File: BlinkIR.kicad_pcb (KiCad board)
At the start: 2 copper layers, 12 parts, among them U1 ATtiny10-TS

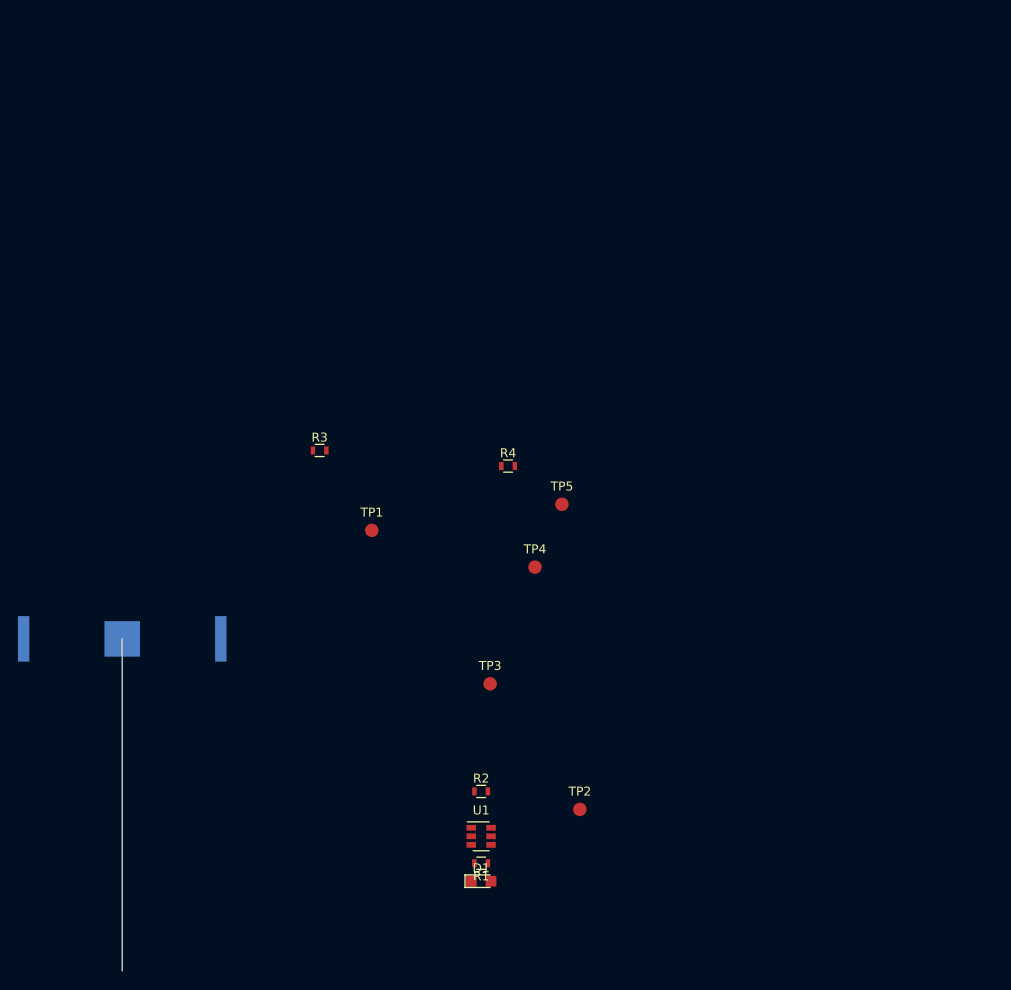
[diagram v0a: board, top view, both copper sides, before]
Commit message: software retargeted to ATTiny10 and dropped uart Schmatic work finished rev1
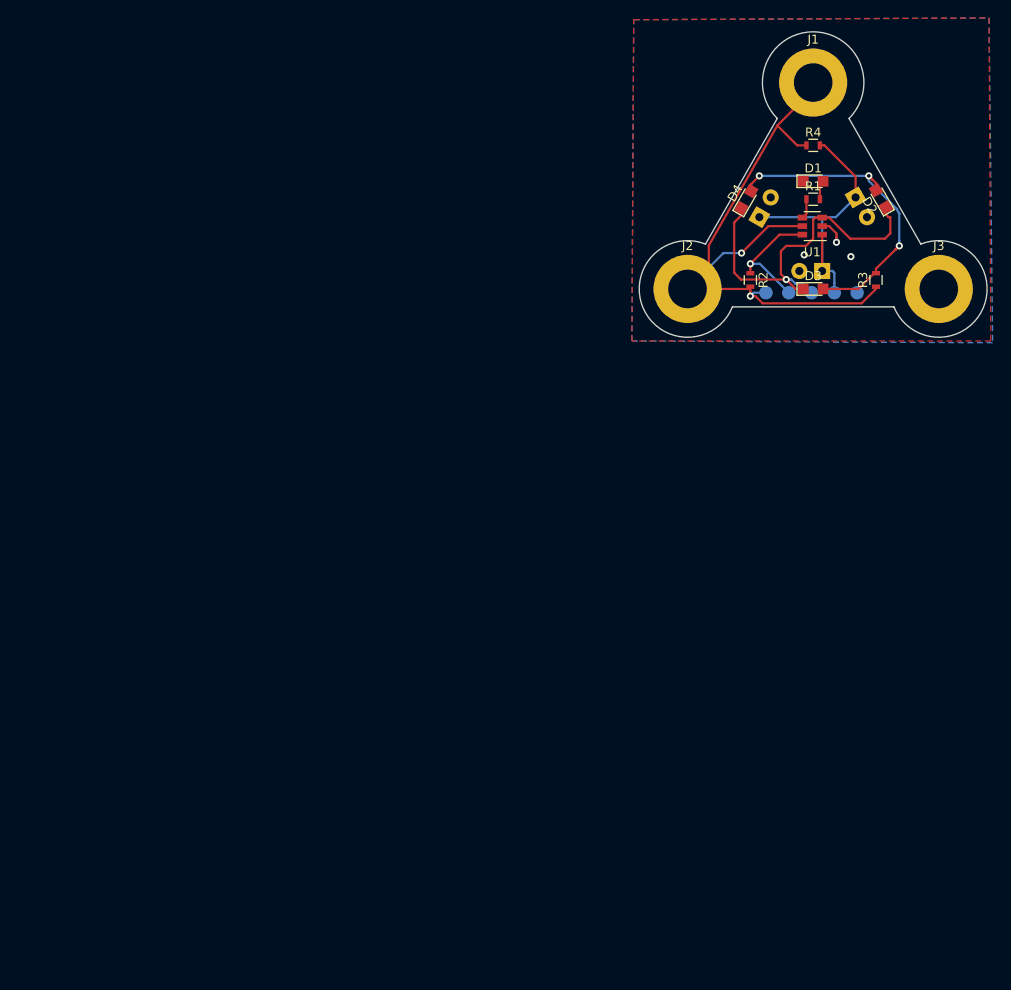
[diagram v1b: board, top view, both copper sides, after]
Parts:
- removed BT1: Battery_Cell, Battery_Holders:Keystone_3034_1x20mm-CoinCell
- added D2: LED, LEDs:LED_0805, F.Cu at (191.6, 64.0)
- added D3: LED, LEDs:LED_0805, F.Cu at (184.0, 74.0)
- added D4: LED, LEDs:LED_0805, F.Cu at (176.6, 64.0)
- added J1: Conn_01x01, Mounting_Holes:MountingHole_4.3mm_M4_ISO7380_Pad, F.Cu at (184.0, 51.0)
- added J2: Conn_01x01, Mounting_Holes:MountingHole_4.3mm_M4_ISO7380_Pad, F.Cu at (170.0, 74.0)
- added J3: Conn_01x01, Mounting_Holes:MountingHole_4.3mm_M4_ISO7380_Pad, F.Cu at (198.0, 74.0)
- added Q1: Q_Photo_NPN, LEDs:LED_D3.0mm_Horizontal_O1.27mm_Z2.0mm, B.Cu at (185.0, 72.0)
- added Q2: Q_Photo_NPN, LEDs:LED_D3.0mm_Horizontal_O1.27mm_Z2.0mm, B.Cu at (178.0, 66.0)
- added Q3: Q_Photo_NPN, LEDs:LED_D3.0mm_Horizontal_O1.27mm_Z2.0mm, B.Cu at (188.7, 63.8)
- TP1, TP2, TP3, TP4, TP5: moved to B.Cu
- moved D1 86.3 mm to (184.0, 62.0)
- moved R1 82.7 mm to (184.0, 64.0), turned to 0 degrees
- moved U1 77.4 mm to (183.9, 67.0), turned to 180 degrees
- moved R3 64.8 mm to (191.0, 73.0), turned to 90 degrees
- moved R2 64.4 mm to (177.0, 73.0), turned to 270 degrees
- moved TP2 62.1 mm to (181.3, 74.4)
- moved TP3 58.1 mm to (186.4, 74.4)
- moved TP1 51.3 mm to (178.7, 74.4)
- moved R4 49.3 mm to (184.0, 58.0)
- moved TP4 43.4 mm to (183.8, 74.4)
- moved TP5 40.5 mm to (188.9, 74.4)
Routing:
- net VCC: track 0.00 -> 72.8 mm, vias 0 -> 2
- net /SEND_BLINK: track 0.00 -> 42.3 mm, vias 0 -> 1
- net Net-(D2-Pad2): track 0.00 -> 37.6 mm, vias 0 -> 3
- net /SENCE_BLINK: track 0.00 -> 33.1 mm
- net /RESET: track 0.00 -> 13.8 mm, vias 0 -> 1
- net GND: track 0.00 -> 2.92 mm, vias 0 -> 3
- net /BLINK: track 0.00 -> 2.24 mm
- net Net-(D1-Pad2): track 0.00 -> 2.14 mm
- added copper zone on B.Cu, net GND
- added copper zone on F.Cu, net GND
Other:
- board outline added: 38.8 x 34 mm

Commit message: Finished PCB and generated Gerber
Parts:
- added G***: LOGO, Silks:toside, F.Cu at (183.8, 64.0)
- added G***: LOGO, Silks:bottomside, B.Cu at (183.6, 67.8)
